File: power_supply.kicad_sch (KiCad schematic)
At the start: 18 parts, among them J1 Разъём к автомобилю 2x16 (32 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, U6 MC78M05CDTG, U7 AMS1117-3.3

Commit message: all unit test pass
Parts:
- C1: value 470uF -> 470u
- C11: value 100uF -> 100u
- C16, C17, C18, C19, C2: value 100nF -> 100n
- C20: value 1uF -> 1u
- C3, C4: value 10uF -> 10u
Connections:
- net GND: now also D2.2 (A), D5.2 (A); no longer D2.1 (K), D5.1 (K)
- net V5_SENS: now also D4.1 (K), D5.1 (K); no longer D4.2 (A), D5.2 (A)
- net VBAT_IN: now also D1.2 (A); no longer D1.1 (K)
- net VBAT_PROT: now also D1.1 (K); no longer D1.2 (A)
- net VCC_12V: now also D2.1 (K); no longer D2.2 (A)
- net VCC_5V: now also D4.2 (A); no longer D4.1 (K)
- net COND_RAW renamed COND_IN_RAW
- net SOLAR_RAW renamed SOLAR_IN_RAW

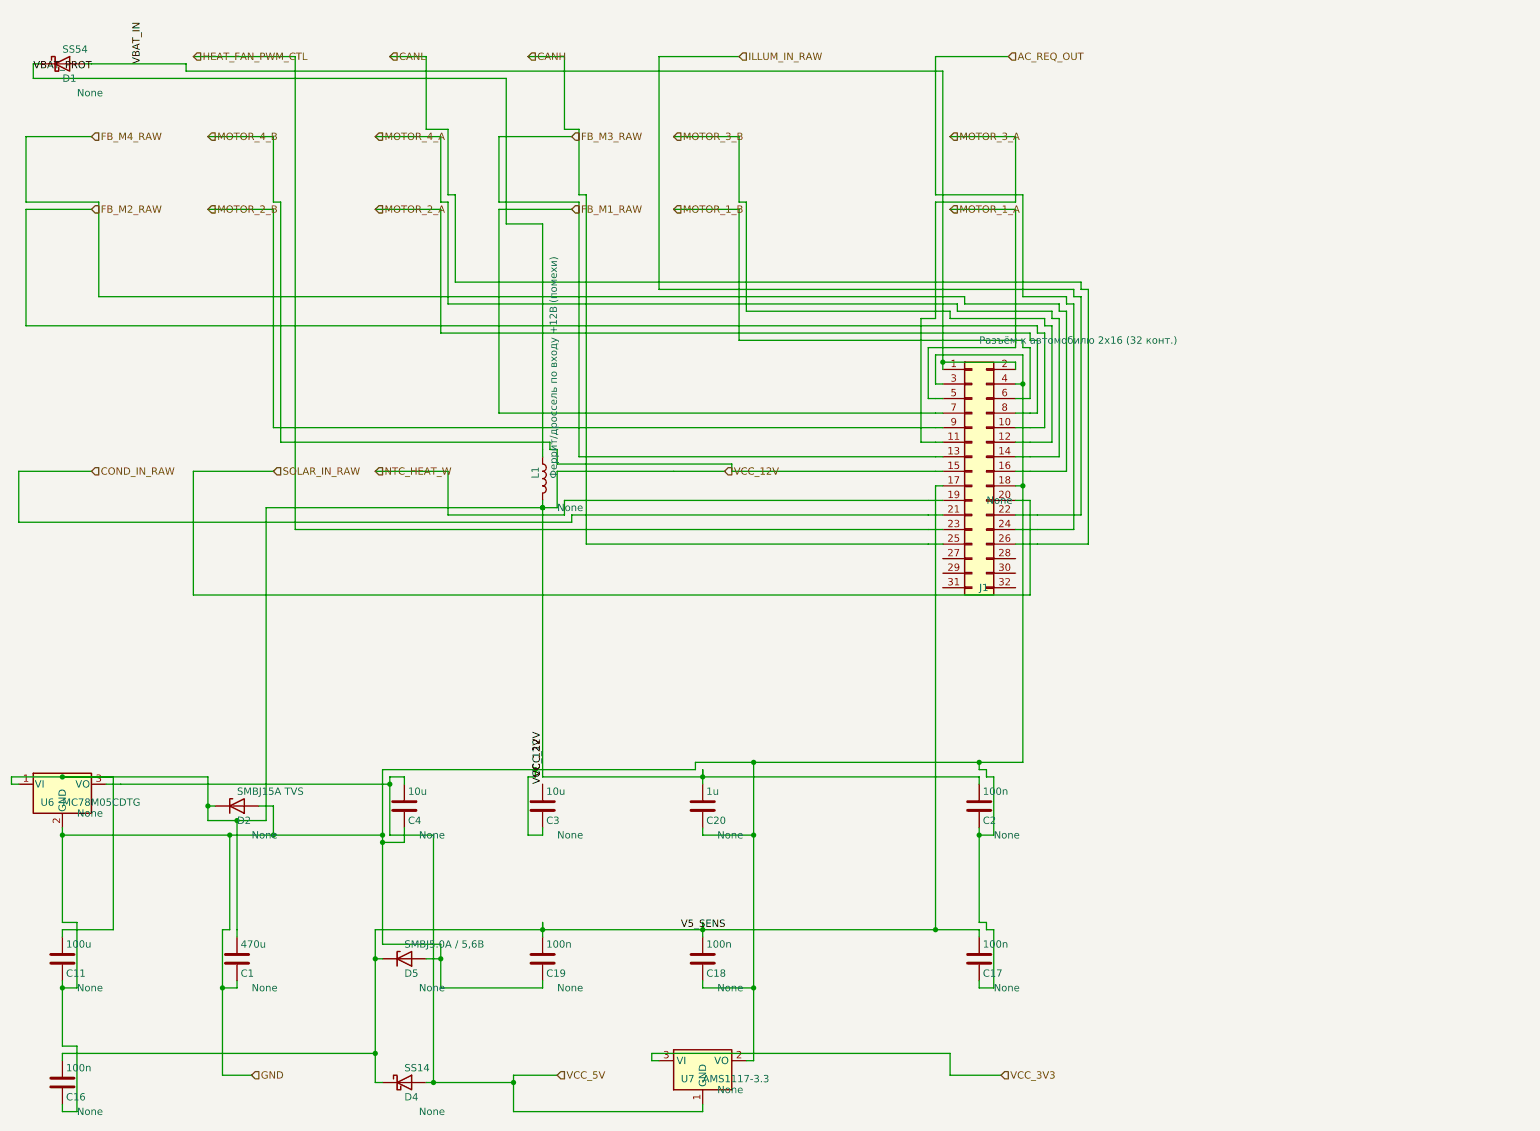
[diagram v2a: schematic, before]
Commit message: optimazed load to kicad
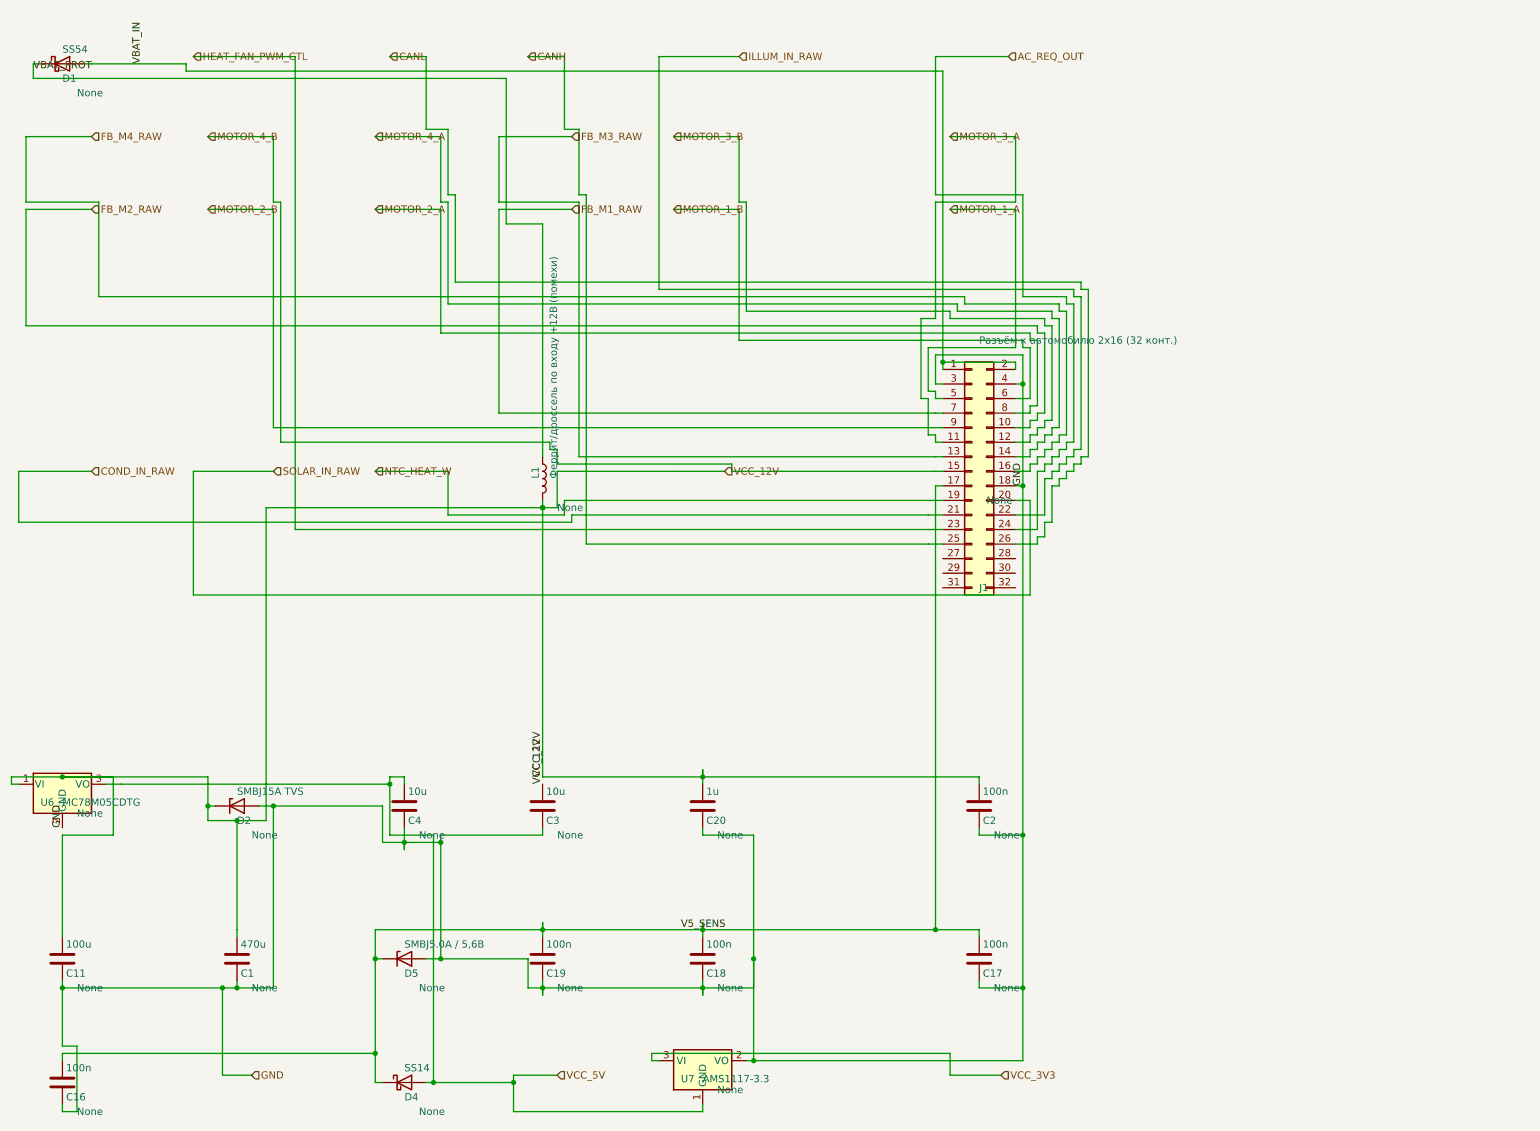
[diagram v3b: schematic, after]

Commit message: tests_fix
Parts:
- C1, C11, C16, C17, C18, C19, C2, C20, C3, C4, D1, D2, D4, D5, J1, L1, U6, U7: hierarchy_path (none) -> /c5a034c1-1f54-4e7e-8711-0930d2b4314e/ecb36219-f9c1-4fc9-9c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
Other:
- title: (none) -> climate_control_niva_travel

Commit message: refactoring
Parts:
- C1, C11, C16, C17, C18, C19, C2, C20, C3, C4, D1, D2, D4, D5, J1, L1, U6, U7: hierarchy_path /c5a034c1-1f54-4e7e-8711-0930d2b4314e/ecb36219-f9c1-4fc9-9c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 -> (none)
